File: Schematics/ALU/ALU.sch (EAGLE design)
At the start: 65 parts

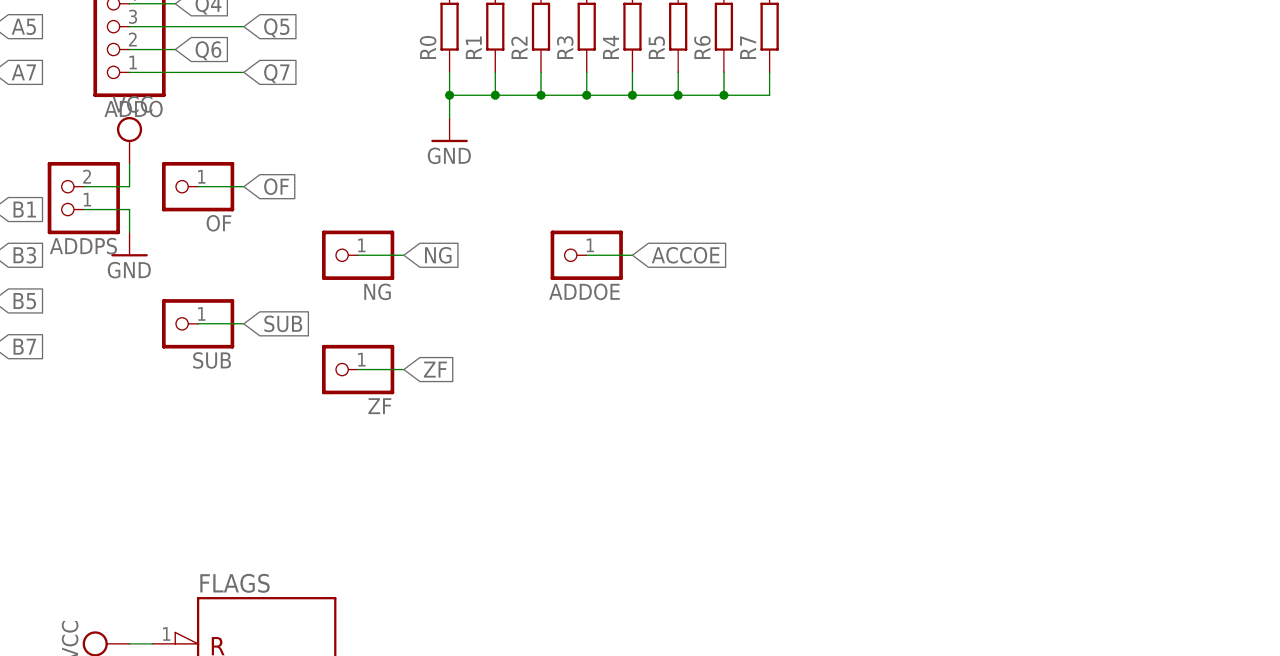
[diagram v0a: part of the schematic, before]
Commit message: Fixed Adder inputs and added LEDs for ZF, OF and NF.
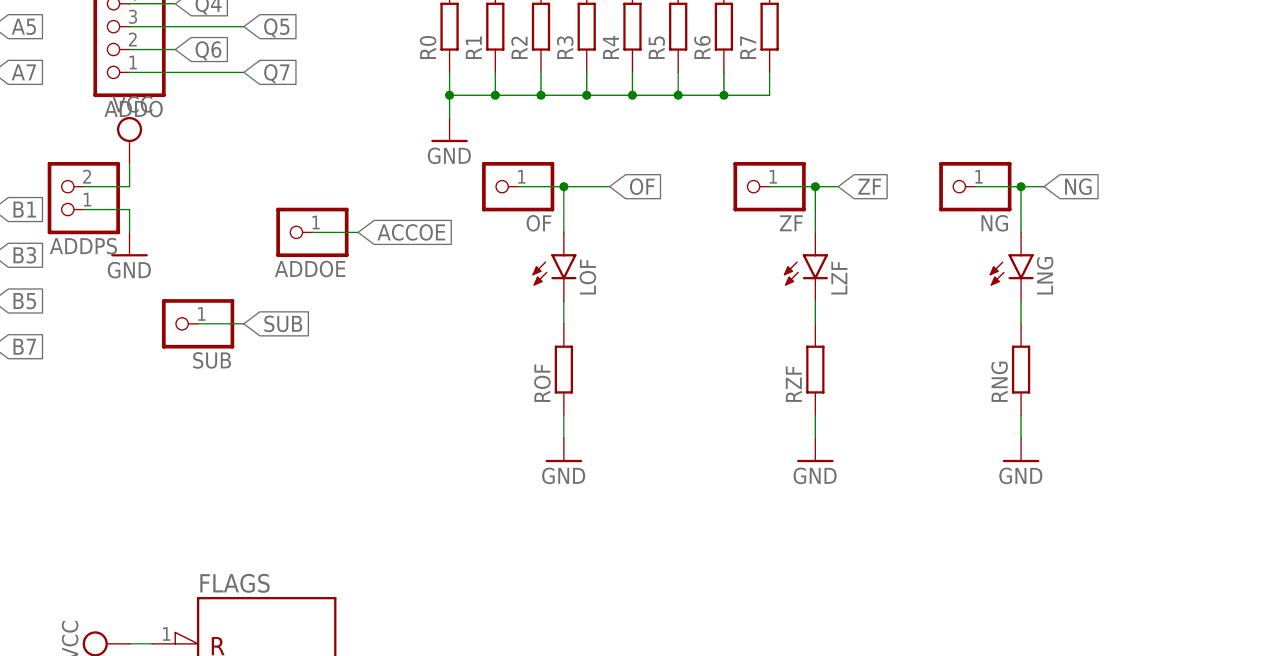
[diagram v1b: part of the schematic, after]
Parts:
- added LNG, LOF, LZF: (no value), led:LED5MM
- added RNG, ROF, RZF: (no value), rcl:R-EU_0204/7
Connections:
- new net N$1: LOF.C, ROF.2
- new net N$2: LZF.C, RZF.2
- new net N$3: LNG.C, RNG.2
- net GND: now also RNG.1, ROF.1, RZF.1
- net NG: now also LNG.A
- net OF: now also LOF.A
- net ZF: now also LZF.A
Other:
- moved on the sheet: ADDOE, NG, OF, ZF
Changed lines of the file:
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@@
 <part name="FLAG" library="pinhead" library_urn="urn:adsk.eagle:library:325" deviceset="PINHD-2X3" device="" package3d_urn="urn:adsk.eagle:package:22462/2"/>
 <part name="CONTROL" library="pinhead" library_urn="urn:adsk.eagle:library:325" deviceset="PINHD-2X7" device="" package3d_urn="urn:adsk.eagle:package:22478/2"/>
+<part name="LOF" library="led" library_urn="urn:adsk.eagle:library:259" deviceset="LED" device="5MM" package3d_urn="urn:adsk.eagle:package:15799/2"/>
+<part name="LZF" library="led" library_urn="urn:adsk.eagle:library:259" deviceset="LED" device="5MM" package3d_urn="urn:adsk.eagle:package:15799/2"/>
+<part name="LNG" library="led" library_urn="urn:adsk.eagle:library:259" deviceset="LED" device="5MM" package3d_urn="urn:adsk.eagle:package:15799/2"/>
+<part name="ROF" library="rcl" library_urn="urn:adsk.eagle:library:334" deviceset="R-EU_" device="0204/7" package3d_urn="urn:adsk.eagle:package:23498/2"/>
+<part name="GND13" library="supply1" library_urn="urn:adsk.eagle:library:371" deviceset="GND" device=""/>
+<part name="RZF" library="rcl" library_urn="urn:adsk.eagle:library:334" deviceset="R-EU_" device="0204/7" package3d_urn="urn:adsk.eagle:package:23498/2"/>
+<part name="GND14" library="supply1" library_urn="urn:adsk.eagle:library:371" deviceset="GND" device=""/>
+<part name="RNG" library="rcl" library_urn="urn:adsk.eagle:library:334" deviceset="R-EU_" device="0204/7" package3d_urn="urn:adsk.eagle:package:23498/2"/>
+<part name="GND15" library="supply1" library_urn="urn:adsk.eagle:library:371" deviceset="GND" device=""/>
 </parts>
 <sheets>
@@
 <attribute name="VALUE" x="261.62" y="208.28" size="1.778" layer="96"/>
 </instance>
-<instance part="OF" gate="G$1" x="269.24" y="218.44" smashed="yes" rot="R180">
-<attribute name="NAME" x="275.59" y="215.265" size="1.778" layer="95" rot="R180"/>
-<attribute name="VALUE" x="275.59" y="223.52" size="1.778" layer="96" rot="R180"/>
+<instance part="OF" gate="G$1" x="304.8" y="218.44" smashed="yes" rot="R180">
+<attribute name="NAME" x="311.15" y="215.265" size="1.778" layer="95" rot="R180"/>
+<attribute name="VALUE" x="311.15" y="223.52" size="1.778" layer="96" rot="R180"/>
 </instance>
 <instance part="SUB" gate="G$1" x="269.24" y="203.2" smashed="yes" rot="R180">
@@
 <attribute name="VALUE" x="297.18" y="220.98" size="1.778" layer="96"/>
 </instance>
-<instance part="NG" gate="G$1" x="287.02" y="210.82" smashed="yes" rot="R180">
-<attribute name="NAME" x="293.37" y="207.645" size="1.778" layer="95" rot="R180"/>
-<attribute name="VALUE" x="293.37" y="215.9" size="1.778" layer="96" rot="R180"/>
-</instance>
-<instance part="ZF" gate="G$1" x="287.02" y="198.12" smashed="yes" rot="R180">
-<attribute name="NAME" x="293.37" y="194.945" size="1.778" layer="95" rot="R180"/>
-<attribute name="VALUE" x="293.37" y="203.2" size="1.778" layer="96" rot="R180"/>
+<instance part="NG" gate="G$1" x="355.6" y="218.44" smashed="yes" rot="R180">
+<attribute name="NAME" x="361.95" y="215.265" size="1.778" layer="95" rot="R180"/>
+<attribute name="VALUE" x="361.95" y="223.52" size="1.778" layer="96" rot="R180"/>
+</instance>
+<instance part="ZF" gate="G$1" x="332.74" y="218.44" smashed="yes" rot="R180">
+<attribute name="NAME" x="339.09" y="215.265" size="1.778" layer="95" rot="R180"/>
+<attribute name="VALUE" x="339.09" y="223.52" size="1.778" layer="96" rot="R180"/>
 </instance>
 <instance part="CMPL" gate="1" x="208.28" y="160.02" smashed="yes">
@@
 <attribute name="VALUE" x="258.445" y="165.735" size="1.778" layer="96" rot="R90"/>
 </instance>
-<instance part="ADDOE" gate="G$1" x="312.42" y="210.82" smashed="yes" rot="R180">
-<attribute name="NAME" x="318.77" y="207.645" size="1.778" layer="95" rot="R180"/>
-<attribute name="VALUE" x="318.77" y="215.9" size="1.778" layer="96" rot="R180"/>
+<instance part="ADDOE" gate="G$1" x="281.94" y="213.36" smashed="yes" rot="R180">
+<attribute name="NAME" x="288.29" y="210.185" size="1.778" layer="95" rot="R180"/>
+<attribute name="VALUE" x="288.29" y="218.44" size="1.778" layer="96" rot="R180"/>
 </instance>
 <instance part="FLAG" gate="A" x="340.36" y="129.54" smashed="yes">
@@
 <attribute name="NAME" x="280.67" y="86.995" size="1.778" layer="95"/>
 <attribute name="VALUE" x="280.67" y="63.5" size="1.778" layer="96"/>
+</instance>
+<instance part="LOF" gate="G$1" x="312.42" y="210.82" smashed="yes">
+<attribute name="NAME" x="315.976" y="206.248" size="1.778" layer="95" rot="R90"/>
+<attribute name="VALUE" x="318.135" y="206.248" size="1.778" layer="96" rot="R90"/>
+</instance>
+<instance part="LZF" gate="G$1" x="340.36" y="210.82" smashed="yes">
+<attribute name="NAME" x="343.916" y="206.248" size="1.778" layer="95" rot="R90"/>
+<attribute name="VALUE" x="346.075" y="206.248" size="1.778" layer="96" rot="R90"/>
+</instance>
+<instance part="LNG" gate="G$1" x="363.22" y="210.82" smashed="yes">
+<attribute name="NAME" x="366.776" y="206.248" size="1.778" layer="95" rot="R90"/>
+<attribute name="VALUE" x="368.935" y="206.248" size="1.778" layer="96" rot="R90"/>
+</instance>
+<instance part="ROF" gate="G$1" x="312.42" y="198.12" smashed="yes" rot="R90">
+<attribute name="NAME" x="310.9214" y="194.31" size="1.778" layer="95" rot="R90"/>
+<attribute name="VALUE" x="315.722" y="194.31" size="1.778" layer="96" rot="R90"/>
+</instance>
+<instance part="GND13" gate="1" x="312.42" y="187.96" smashed="yes">
+<attribute name="VALUE" x="309.88" y="185.42" size="1.778" layer="96"/>
+</instance>
+<instance part="RZF" gate="G$1" x="340.36" y="198.12" smashed="yes" rot="R90">
+<attribute name="NAME" x="338.8614" y="194.31" size="1.778" layer="95" rot="R90"/>
+<attribute name="VALUE" x="343.662" y="194.31" size="1.778" layer="96" rot="R90"/>
+</instance>
+<instance part="GND14" gate="1" x="340.36" y="187.96" smashed="yes">
+<attribute name="VALUE" x="337.82" y="185.42" size="1.778" layer="96"/>
+</instance>
+<instance part="RNG" gate="G$1" x="363.22" y="198.12" smashed="yes" rot="R90">
+<attribute name="NAME" x="361.7214" y="194.31" size="1.778" layer="95" rot="R90"/>
+<attribute name="VALUE" x="366.522" y="194.31" size="1.778" layer="96" rot="R90"/>
+</instance>
+<instance part="GND15" gate="1" x="363.22" y="187.96" smashed="yes">
+<attribute name="VALUE" x="360.68" y="185.42" size="1.778" layer="96"/>
 </instance>
 </instances>
@@
 <pinref part="GND12" gate="1" pin="GND"/>
 </segment>
+<segment>
+<pinref part="GND13" gate="1" pin="GND"/>
+<pinref part="ROF" gate="G$1" pin="1"/>
+<wire x1="312.42" y1="190.5" x2="312.42" y2="193.04" width="0.1524" layer="91"/>
+</segment>
+<segment>
+<pinref part="GND14" gate="1" pin="GND"/>
+<pinref part="RZF" gate="G$1" pin="1"/>
+<wire x1="340.36" y1="190.5" x2="340.36" y2="193.04" width="0.1524" layer="91"/>
+</segment>
+<segment>
+<pinref part="GND15" gate="1" pin="GND"/>
+<pinref part="RNG" gate="G$1" pin="1"/>
+<wire x1="363.22" y1="190.5" x2="363.22" y2="193.04" width="0.1524" layer="91"/>
+</segment>
 </net>
 <net name="A0" class="0">
@@
 <segment>
 <pinref part="OF" gate="G$1" pin="1"/>
-<wire x1="271.78" y1="218.44" x2="276.86" y2="218.44" width="0.1524" layer="91"/>
-<label x="276.86" y="218.44" size="1.778" layer="95" xref="yes"/>
+<wire x1="307.34" y1="218.44" x2="312.42" y2="218.44" width="0.1524" layer="91"/>
+<label x="317.5" y="218.44" size="1.778" layer="95" xref="yes"/>
+<pinref part="LOF" gate="G$1" pin="A"/>
+<wire x1="312.42" y1="218.44" x2="317.5" y2="218.44" width="0.1524" layer="91"/>
+<wire x1="312.42" y1="213.36" x2="312.42" y2="218.44" width="0.1524" layer="91"/>
+<junction x="312.42" y="218.44"/>
 </segment>
 <segment>
@@
 <segment>
 <pinref part="NG" gate="G$1" pin="1"/>
-<wire x1="294.64" y1="210.82" x2="289.56" y2="210.82" width="0.1524" layer="91"/>
-<label x="294.64" y="210.82" size="1.778" layer="95" xref="yes"/>
+<wire x1="365.76" y1="218.44" x2="363.22" y2="218.44" width="0.1524" layer="91"/>
+<label x="365.76" y="218.44" size="1.778" layer="95" xref="yes"/>
+<pinref part="LNG" gate="G$1" pin="A"/>
+<wire x1="363.22" y1="218.44" x2="358.14" y2="218.44" width="0.1524" layer="91"/>
+<wire x1="363.22" y1="213.36" x2="363.22" y2="218.44" width="0.1524" layer="91"/>
+<junction x="363.22" y="218.44"/>
 </segment>
 <segment>
@@
 <segment>
 <pinref part="ZF" gate="G$1" pin="1"/>
-<wire x1="294.64" y1="198.12" x2="289.56" y2="198.12" width="0.1524" layer="91"/>
-<label x="294.64" y="198.12" size="1.778" layer="95" xref="yes"/>
+<wire x1="342.9" y1="218.44" x2="340.36" y2="218.44" width="0.1524" layer="91"/>
+<label x="342.9" y="218.44" size="1.778" layer="95" xref="yes"/>
+<pinref part="LZF" gate="G$1" pin="A"/>
+<wire x1="340.36" y1="218.44" x2="335.28" y2="218.44" width="0.1524" layer="91"/>
+<wire x1="340.36" y1="213.36" x2="340.36" y2="218.44" width="0.1524" layer="91"/>
+<junction x="340.36" y="218.44"/>
 </segment>
 <segment>
@@
 <segment>
 <pinref part="ADDOE" gate="G$1" pin="1"/>
-<wire x1="314.96" y1="210.82" x2="320.04" y2="210.82" width="0.1524" layer="91"/>
-<label x="320.04" y="210.82" size="1.778" layer="95" xref="yes"/>
+<wire x1="284.48" y1="213.36" x2="289.56" y2="213.36" width="0.1524" layer="91"/>
+<label x="289.56" y="213.36" size="1.778" layer="95" xref="yes"/>
 </segment>
 <segment>
@@
 </segment>
 </net>
+<net name="N$1" class="0">
+<segment>
+<pinref part="ROF" gate="G$1" pin="2"/>
+<pinref part="LOF" gate="G$1" pin="C"/>
+<wire x1="312.42" y1="203.2" x2="312.42" y2="205.74" width="0.1524" layer="91"/>
+</segment>
+</net>
+<net name="N$2" class="0">
+<segment>
+<pinref part="RZF" gate="G$1" pin="2"/>
+<pinref part="LZF" gate="G$1" pin="C"/>
+<wire x1="340.36" y1="203.2" x2="340.36" y2="205.74" width="0.1524" layer="91"/>
+</segment>
+</net>
+<net name="N$3" class="0">
+<segment>
+<pinref part="RNG" gate="G$1" pin="2"/>
+<pinref part="LNG" gate="G$1" pin="C"/>
+<wire x1="363.22" y1="203.2" x2="363.22" y2="205.74" width="0.1524" layer="91"/>
+</segment>
+</net>
